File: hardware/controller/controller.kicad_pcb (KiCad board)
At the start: 2 copper layers, 23 parts, among them J1 Screw_Terminal_01x02, J2 Screw_Terminal_01x02, J3 Screw_Terminal_01x02, J4 GROVE-CONNECTOR-DIP-90D_4P-2.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, T1 NMOSFETSOT23, T2 NMOSFETSOT23, T3 NMOSFETSOT23, T4 NMOSFETTO252, T5 NMOSFETTO252, U1 RO3.3-9S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

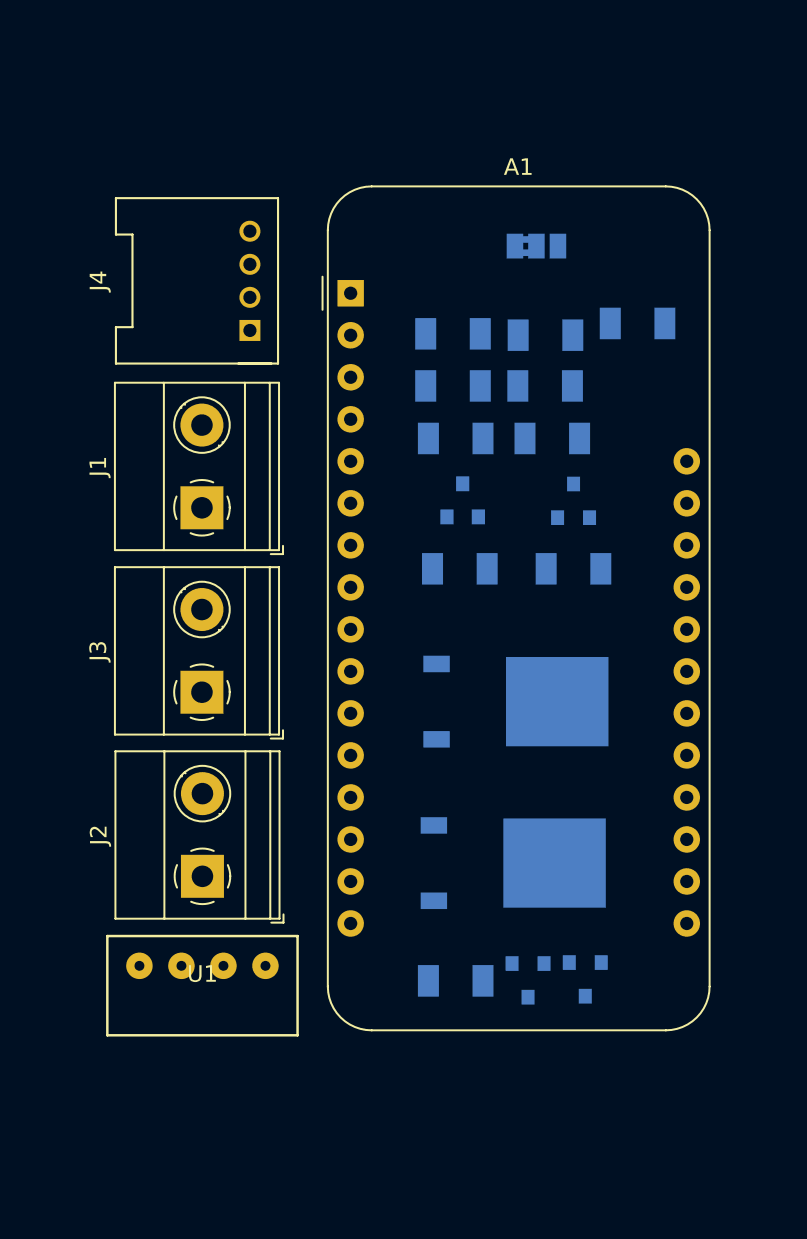
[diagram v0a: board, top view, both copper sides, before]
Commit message: Add overkill controller version
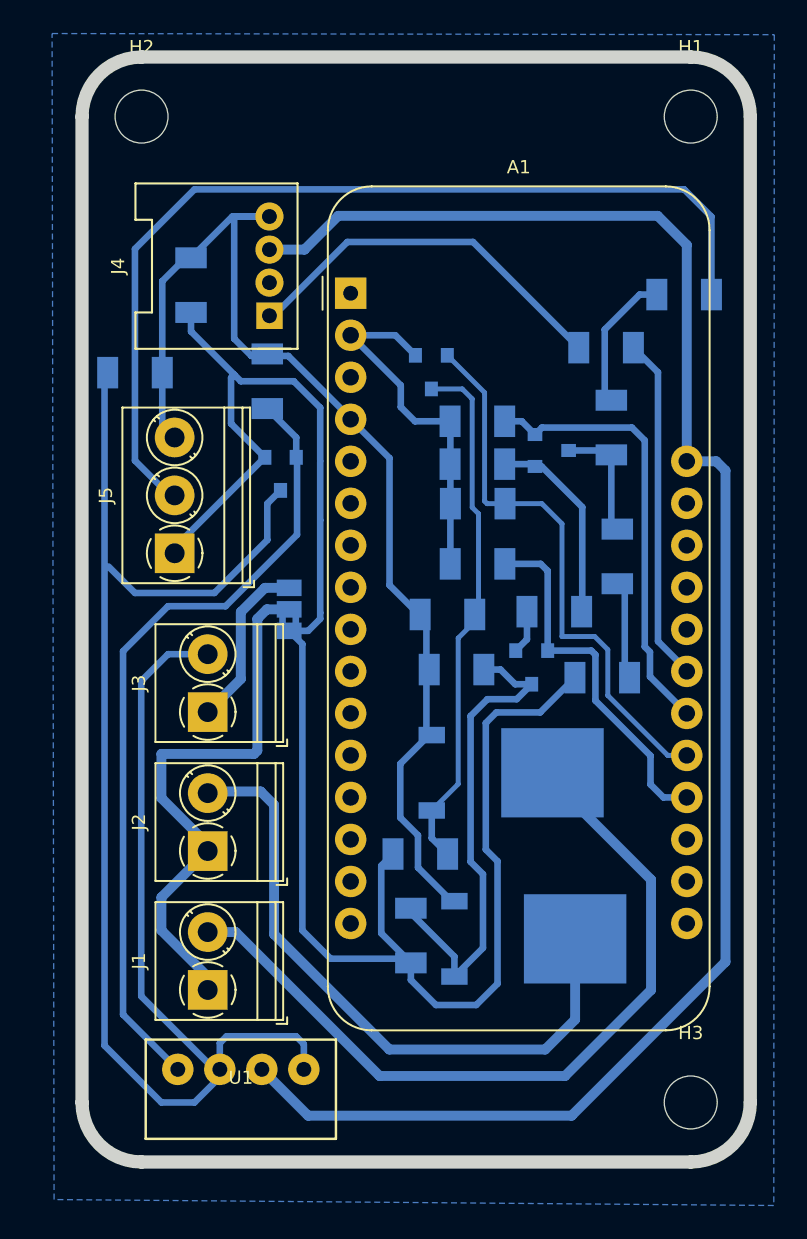
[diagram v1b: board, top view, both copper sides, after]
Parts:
- added H1: MountingHole, MountingHole:MountingHole_3.2mm_M3, F.Cu at (151.2, 58.8)
- added H2: MountingHole, MountingHole:MountingHole_3.2mm_M3, F.Cu at (118.0, 58.8)
- added H3: MountingHole, MountingHole:MountingHole_3.2mm_M3, F.Cu at (151.2, 118.4)
- added J5: Screw_Terminal_01x03, TerminalBlock_Phoenix:TerminalBlock_Phoenix_PT-1,5-3-3.5-H_1x03_P3.50mm_Horizontal, F.Cu at (120.0, 85.2)
- added R10: 0, fab:fab-R1206FAB, B.Cu at (142.9, 88.7)
- added R11: 0, fab:fab-R1206FAB, B.Cu at (138.3, 79.8)
- added R12: 0, fab:fab-R1206FAB, B.Cu at (145.8, 92.7)
- added R13: 0, fab:fab-R1206FAB, B.Cu at (117.6, 74.3)
- added R14: 0, fab:fab-R1206FAB, B.Cu at (146.4, 77.6)
- added R15: 0, fab:fab-R1206FAB, B.Cu at (150.8, 69.6)
- added R9: 470Ω, fab:fab-R1206FAB, B.Cu at (146.1, 72.8)
- J1, J2, J3: footprint TerminalBlock_Phoenix:TerminalBlock_Phoenix_MKDS-1,5-2_1x02_P5.00mm_Horizontal -> TerminalBlock_Phoenix:TerminalBlock_Phoenix_PT-1,5-2-3.5-H_1x02_P3.50mm_Horizontal
- moved T2 37.9 mm to (135.5, 74.2)
- moved R2 37.2 mm to (134.3, 108.3), turned to 90 degrees
- moved J1 29.2 mm to (122.0, 111.6)
- moved JP1 26.6 mm to (126.9, 88.6), turned to 90 degrees
- moved R4 26.4 mm to (134.8, 103.4), turned to 0 degrees
- moved C2 23.6 mm to (121.0, 69.0), turned to 90 degrees
- moved R8 22.2 mm to (136.5, 88.9)
- moved T1 18.9 mm to (141.6, 92.1)
- moved R1 17.5 mm to (138.3, 85.8)
- moved R7 14.0 mm to (137.0, 92.2)
- moved C1 11.2 mm to (125.6, 74.8), turned to 90 degrees
- moved U2 11.1 mm to (126.4, 80.4), turned to -90 degrees
- moved R3 8.20 mm to (138.3, 82.2)
- moved U1 6.68 mm to (124.0, 116.4)
- moved R5 5.49 mm to (138.3, 77.2)
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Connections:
- A1 pad 1: (no net) -> unconnected-(A1-Pad1)
- A1 pad 10: (no net) -> unconnected-(A1-Pad10)
- A1 pad 11: (no net) -> unconnected-(A1-Pad11)
- A1 pad 12: (no net) -> unconnected-(A1-Pad12)
- A1 pad 13: (no net) -> unconnected-(A1-Pad13)
- A1 pad 14: (no net) -> unconnected-(A1-Pad14)
- A1 pad 15: (no net) -> unconnected-(A1-Pad15)
- A1 pad 16: (no net) -> unconnected-(A1-Pad16)
- A1 pad 17: (no net) -> unconnected-(A1-Pad17)
- A1 pad 18: (no net) -> unconnected-(A1-Pad18)
- A1 pad 19: (no net) -> unconnected-(A1-Pad19)
- A1 pad 23: LEDSTRIP -> Net-(A1-Pad23)
- A1 pad 24: (no net) -> unconnected-(A1-Pad24)
- A1 pad 25: (no net) -> unconnected-(A1-Pad25)
- A1 pad 26: (no net) -> unconnected-(A1-Pad26)
- A1 pad 27: (no net) -> unconnected-(A1-Pad27)
- A1 pad 3: (no net) -> unconnected-(A1-Pad3)
- A1 pad 5: (no net) -> unconnected-(A1-Pad5)
- A1 pad 6: (no net) -> unconnected-(A1-Pad6)
- A1 pad 7: (no net) -> unconnected-(A1-Pad7)
- A1 pad 8: (no net) -> unconnected-(A1-Pad8)
- A1 pad 9: (no net) -> unconnected-(A1-Pad9)
- J4 pad 2: (no net) -> unconnected-(J4-Pad2)
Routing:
- net GND: track 0.00 -> 174.0 mm
- net 5V: track 0.00 -> 109.2 mm
- net VBAT: track 0.00 -> 105.4 mm
- net LASERPWM_H: track 0.00 -> 73.6 mm
- net Net-(C1-Pad1): track 0.00 -> 48.5 mm
- net LIGHTMSFT_1: track 0.00 -> 48.2 mm
- net LIGHTMSFT_2: track 0.00 -> 38.9 mm
- net 3V3: track 0.00 -> 36.7 mm
- net LIGHTMSFT_1_L: track 0.00 -> 34.0 mm
- net VOUT: track 0.00 -> 33.8 mm
- net LIGHTMSFT_1_H: track 0.00 -> 32.0 mm
- net LIGHTMSFT_2_H: track 0.00 -> 29.7 mm
- net LASERPWM_L: track 0.00 -> 26.9 mm
- net LEDSTRIP: track 0.00 -> 23.2 mm
- net LIGHTMSFT_2_L: track 0.00 -> 22.3 mm
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- added copper zone on B.Cu, net GND
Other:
- board outline added: 40.4 x 66.8 mm
- net class Default removed

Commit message: Last version of controller
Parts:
- removed J3: Screw_Terminal_01x02, TerminalBlock_Phoenix:TerminalBlock_Phoenix_PT-1,5-2-3.5-H_1x02_P3.50mm_Horizontal
- removed R13, R15: 0, fab:fab-R1206FAB
- removed R4, R8: 10kΩ, fab:fab-R1206FAB
- removed T2: NMOSFETSOT23, fab:fab-SOT-23
- removed T5: NMOSFETTO252, fab:fab-TO252
- added C3: 1uF, fab:fab-C1206FAB, B.Cu at (140.8, 111.6)
- added C4: 4.7uF, fab:fab-C1206FAB, B.Cu at (142.0, 90.0)
- added C5: 1uF, fab:fab-C1206FAB, B.Cu at (138.0, 101.6)
- added C6: 4.7uF, fab:fab-C1206FAB, B.Cu at (127.6, 108.0)
- added U3: AP7361C-33E, Package_TO_SOT_SMD:SOT-223-3_TabPin2, B.Cu at (139.6, 95.6)
- added U4: AP7361C-33E, Package_TO_SOT_SMD:SOT-223-3_TabPin2, B.Cu at (136.4, 106.4)
- JP1: value SolderJumper_3_Bridged12 -> Jumper_3_Bridged12; footprint Jumper:SolderJumper-3_P1.3mm_Bridged2Bar12_Pad1.0x1.5mm -> Jumper:SolderJumper-3_P1.3mm_Bridged12_RoundedPad1.0x1.5mm
- R3: value 10kΩ -> 0
- moved U1 56.6 mm to (132.0, 60.4), turned to 180 degrees
- moved A1 45.6 mm to (147.4, 111.9), turned to 180 degrees
- moved H3 33.2 mm to (118.0, 118.4)
- moved R12 32.0 mm to (143.2, 60.8), turned to -90 degrees
- moved R2 28.3 mm to (142.5, 81.2), turned to -90 degrees
- moved R7 24.8 mm to (140.4, 116.8), turned to 0 degrees
- moved C2 24.5 mm to (145.2, 65.2), turned to 0 degrees
- moved R14 23.2 mm to (123.2, 78.8), turned to 90 degrees
- moved U2 21.0 mm to (140.0, 64.4), turned to 90 degrees
- moved R3 16.9 mm to (133.6, 98.4), turned to -90 degrees
- moved R6 15.9 mm to (139.6, 71.2), turned to -90 degrees
- moved R10 15.7 mm to (144.4, 104.4), turned to 90 degrees
- moved R9 15.7 mm to (130.4, 72.0), turned to -90 degrees
- moved T4 14.9 mm to (128.8, 116.0), turned to -90 degrees
- moved C1 13.0 mm to (134.4, 65.2), turned to 180 degrees
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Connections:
- net LIGHTMSFT_2_H renamed LIGHTMSFT_H
- A1 pad 20: LIGHTMSFT_2_L -> unconnected-(A1-Pad20)
- A1 pad 21: LIGHTMSFT_1_L -> Net-(A1-Pad21)
- A1 pad 23: Net-(A1-Pad23) -> LIGHTMSFT_L
- A1 pad 26: unconnected-(A1-Pad26) -> VBUS
- J1 pad 1: VOUT -> 3V3_REG_2
- J1 pad 2: LIGHTMSFT_1 -> LIGHTMSFT
- J2 pad 1: VOUT -> 3V3_REG_1
- J2 pad 2: LIGHTMSFT_2 -> LIGHTMSFT
- JP1 pad 1: 5V -> VBAT
- JP1 pad 2: VOUT -> VI
- JP1 pad 3: VIN -> VBUS
- R1 pad 2: LIGHTMSFT_2_L -> LIGHTMSFT_L
- R14 pad 1: LASERPWM_H -> VBAT
- R14 pad 2: LASERPWM_H -> VBAT
- R3 pad 1: 3V3 -> Net-(C4-Pad1)
- R3 pad 2: LIGHTMSFT_1_L -> 3V3_REG_1
- R9 pad 2: Net-(A1-Pad23) -> Net-(A1-Pad21)
- T1 pad 2: LIGHTMSFT_2_L -> LIGHTMSFT_L
- T4 pad 3: LIGHTMSFT_2 -> LIGHTMSFT
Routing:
- net VBAT: track 105.4 -> 53.4 mm
- net LIGHTMSFT_1: track 48.2 -> 0.00 mm
- net LASERPWM_H: track 73.6 -> 29.2 mm
- net Net-(C1-Pad1): track 48.5 -> 7.98 mm
- net LIGHTMSFT: track 0.00 -> 39.8 mm
- net LIGHTMSFT_2: track 38.9 -> 0.00 mm
- net 5V: track 109.2 -> 71.1 mm
- net LIGHTMSFT_1_L: track 34.0 -> 0.00 mm
- net VOUT: track 33.8 -> 0.00 mm
- net LIGHTMSFT_1_H: track 32.0 -> 0.00 mm
- net 3V3_REG_1: track 0.00 -> 28.3 mm
- net LIGHTMSFT_H: track 29.7 -> 58.0 mm
- net VI: track 0.00 -> 25.7 mm
- net LIGHTMSFT_2_L: track 22.3 -> 0.00 mm
- net Net-(A1-Pad23): track 20.9 -> 0.00 mm
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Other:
- board size 40.4 x 66.8 mm -> 37.2 x 66.8 mm

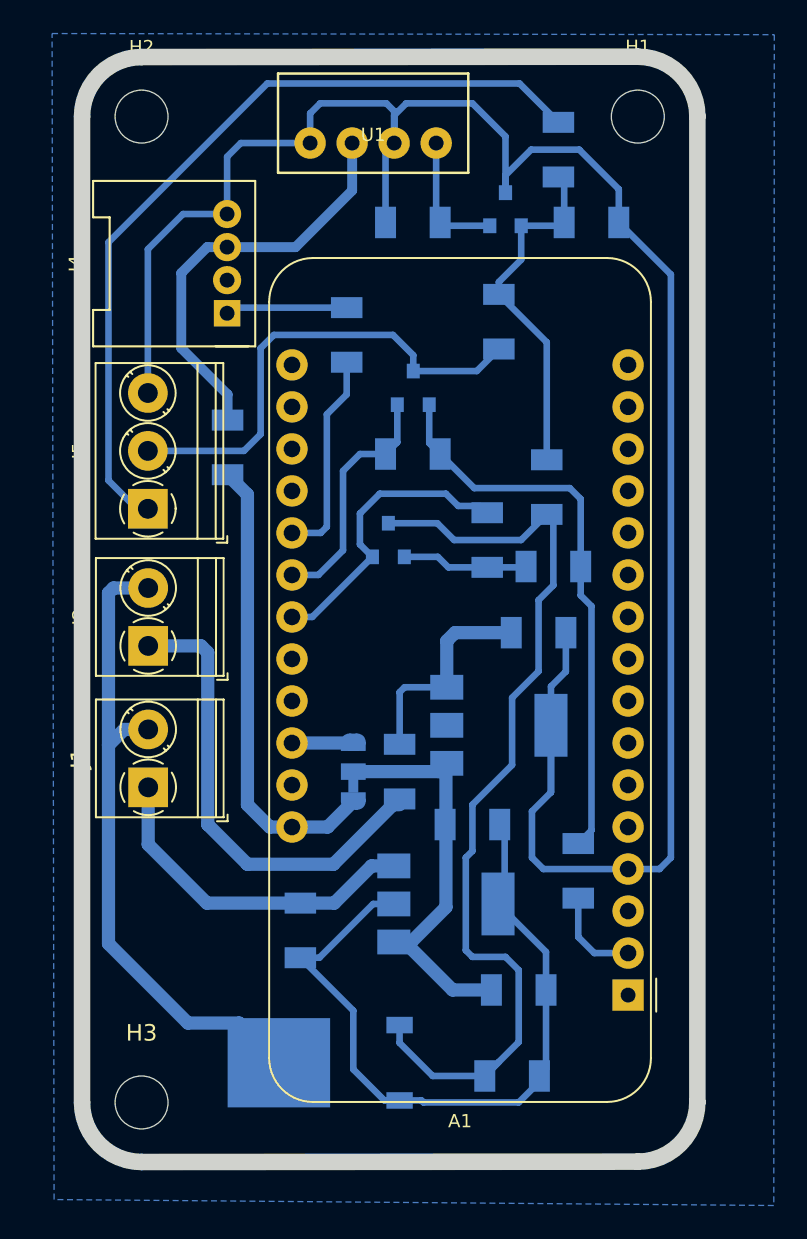
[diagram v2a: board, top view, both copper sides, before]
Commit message: electronics with separate power sources and switch
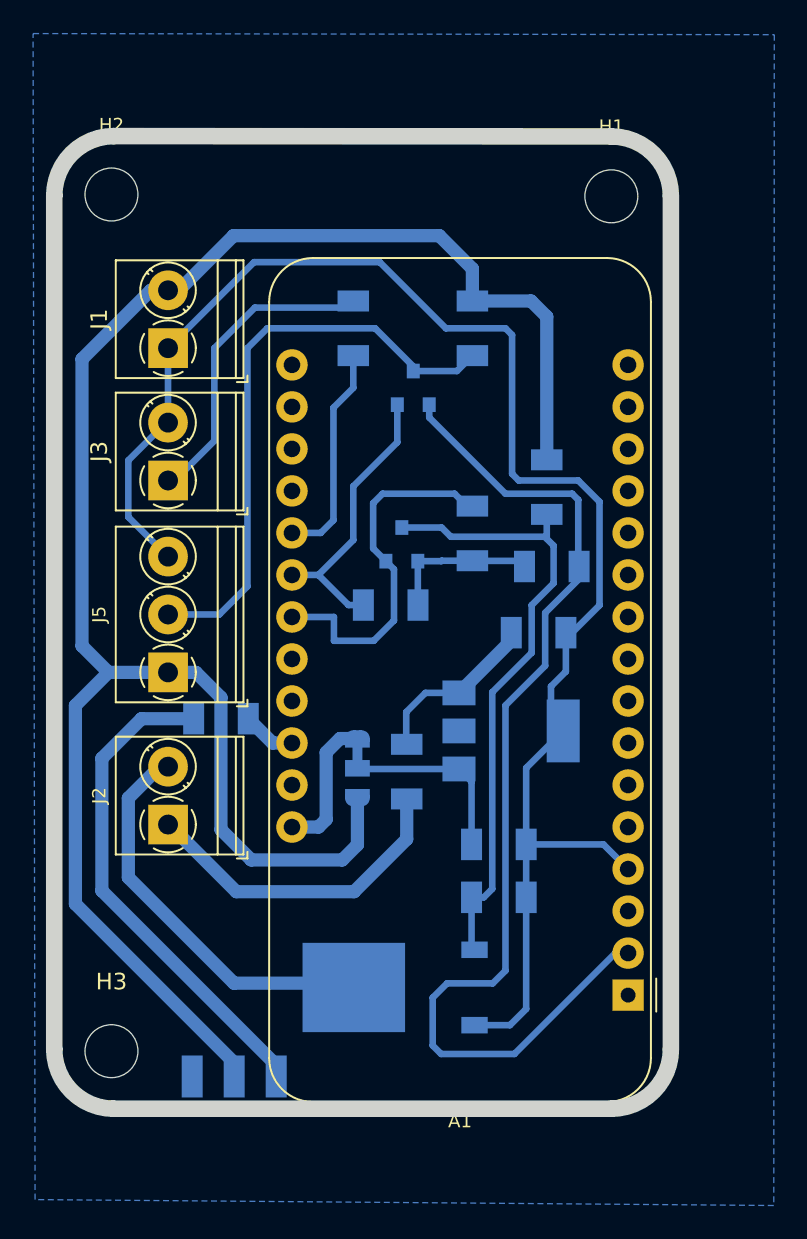
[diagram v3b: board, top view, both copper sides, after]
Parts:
- removed C1, C2: 100nF, fab:fab-C1206FAB
- removed C5: 1uF, fab:fab-C1206FAB
- removed C6: 4.7uF, fab:fab-C1206FAB
- removed J4: GROVE-CONNECTOR-DIP-90D_4P-2.0_, OPL_Connector:HW4-2.0-90D
- removed R10, R11, R12, R14: 0, fab:fab-R1206FAB
- removed U1: RO3.3-9S, Converter_DCDC:Converter_DCDC_RECOM_RO_3.309S
- removed U2: LM3480-5.0, Package_TO_SOT_SMD:SOT-23
- removed U4: AP7361C-33E, Package_TO_SOT_SMD:SOT-223-3_TabPin2
- added J3: Screw_Terminal_01x02, TerminalBlock_Phoenix:TerminalBlock_Phoenix_PT-1,5-2-3.5-H_1x02_P3.50mm_Horizontal, F.Cu at (119.6, 80.8)
- added R4: 0, fab:fab-R1206FAB, B.Cu at (142.8, 86.0)
- added R8: 0, fab:fab-R1206FAB, B.Cu at (122.8, 95.2)
- added SW1: SW_SPDT, fab:fab-SPDTSWITCH, B.Cu at (123.6, 117.2)
- JP1: footprint Jumper:SolderJumper-3_P1.3mm_Bridged12_RoundedPad1.0x1.5mm -> Jumper:SolderJumper-3_P1.3mm_Bridged12_RoundedPad1.0x1.5mm_NumberLabels
- moved J1 26.6 mm to (119.6, 72.8)
- moved J2 10.9 mm to (119.6, 101.6)
- moved R7 10.8 mm to (139.6, 106.0)
- moved J5 9.96 mm to (119.6, 92.4)
- moved R5 9.23 mm to (133.1, 88.3)
- moved C3 8.88 mm to (139.6, 102.8)
- moved T4 6.42 mm to (133.3, 111.4)
- moved H1 5.08 mm to (146.4, 63.6)
- moved H2 5.05 mm to (116.2, 63.5)
- moved H3 3.59 mm to (116.2, 115.3)
- moved R6 1.65 mm to (138.0, 71.6)
- moved R1 0.98 mm to (138.0, 84.0)
- moved T1 0.86 mm to (133.7, 84.7)
- moved U3 0.81 mm to (140.3, 95.9)
- moved R9 0.57 mm to (130.8, 71.6)
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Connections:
- net VI renamed Net-(C3-Pad1)
- A1 pad 26: VBUS -> Net-(A1-Pad26)
- J1 pad 1: 3V3_REG_2 -> GND
- J1 pad 2: LIGHTMSFT -> VBUS
- J5 pad 1: 5V -> VBUS
- R2 pad 1: 5V -> VBUS
- R6 pad 1: 5V -> VBUS
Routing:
- net VBUS: track 3.74 -> 119.5 mm
- net GND: track 173.0 -> 97.5 mm
- net 5V: track 71.1 -> 0.00 mm
- net VBAT: track 53.4 -> 8.55 mm
- net Net-(SW1-Pad1): track 0.00 -> 30.1 mm
- net 3V3: track 47.7 -> 74.0 mm
- net 3V3_REG_2: track 20.7 -> 0.00 mm
- net LIGHTMSFT_H: track 58.0 -> 38.1 mm
- net LIGHTMSFT: track 39.8 -> 24.4 mm
- net Net-(C3-Pad1): track 25.7 -> 11.5 mm
- net LEDSTRIP: track 7.37 -> 19.0 mm
- net 3V3_REG_1: track 28.3 -> 19.9 mm
- net Net-(C1-Pad1): track 7.98 -> 0.00 mm
- net LASERPWM_H: track 29.2 -> 35.6 mm
- net LIGHTMSFT_L: track 17.4 -> 22.5 mm
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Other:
- board size 37.2 x 66.8 mm -> 37.3 x 58.8 mm
